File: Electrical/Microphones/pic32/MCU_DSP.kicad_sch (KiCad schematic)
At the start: 28 parts, among them IC1 PIC32MK0128MCA048-I_Y8X, J1 Conn_01x05_Pin, J2 Conn_01x06, J3 Conn_01x06, J4 Conn_01x05, J5 Conn_01x06, J6 Conn_01x05, J7 UART, SW1 B3F-1020, SW2 SW_SPDT, U1 GSF7002DW

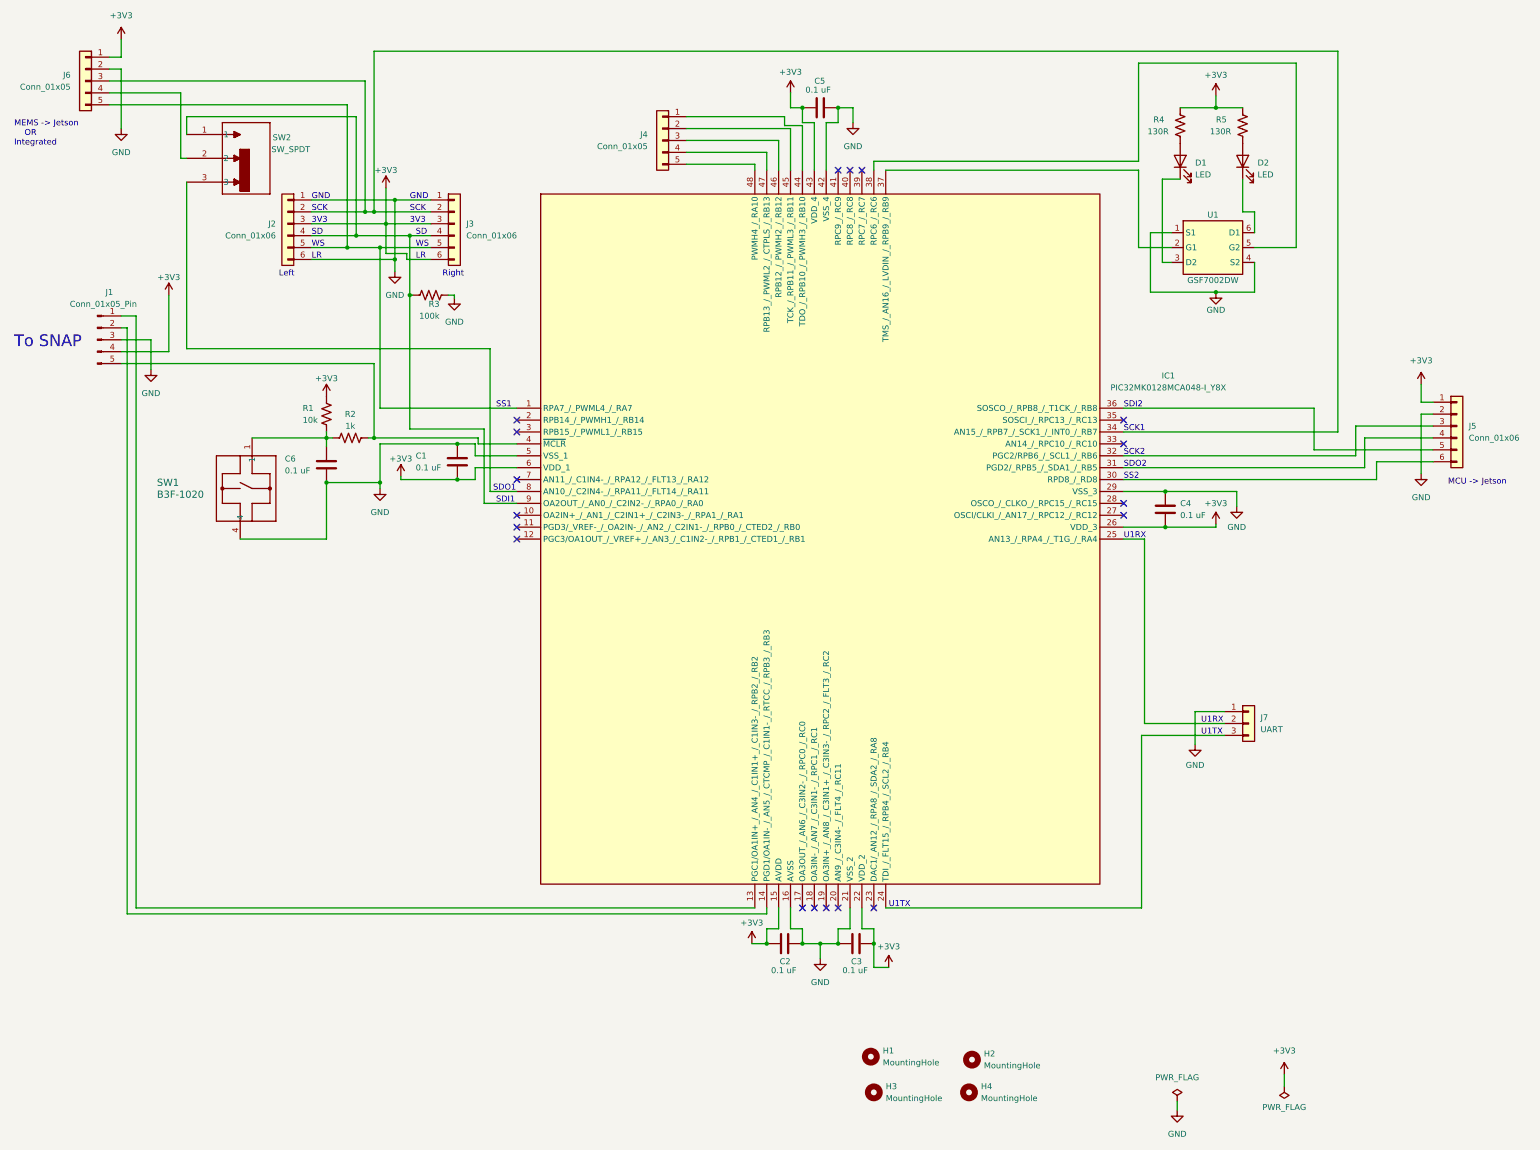
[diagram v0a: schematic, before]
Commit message: Add updated Mic MCU board
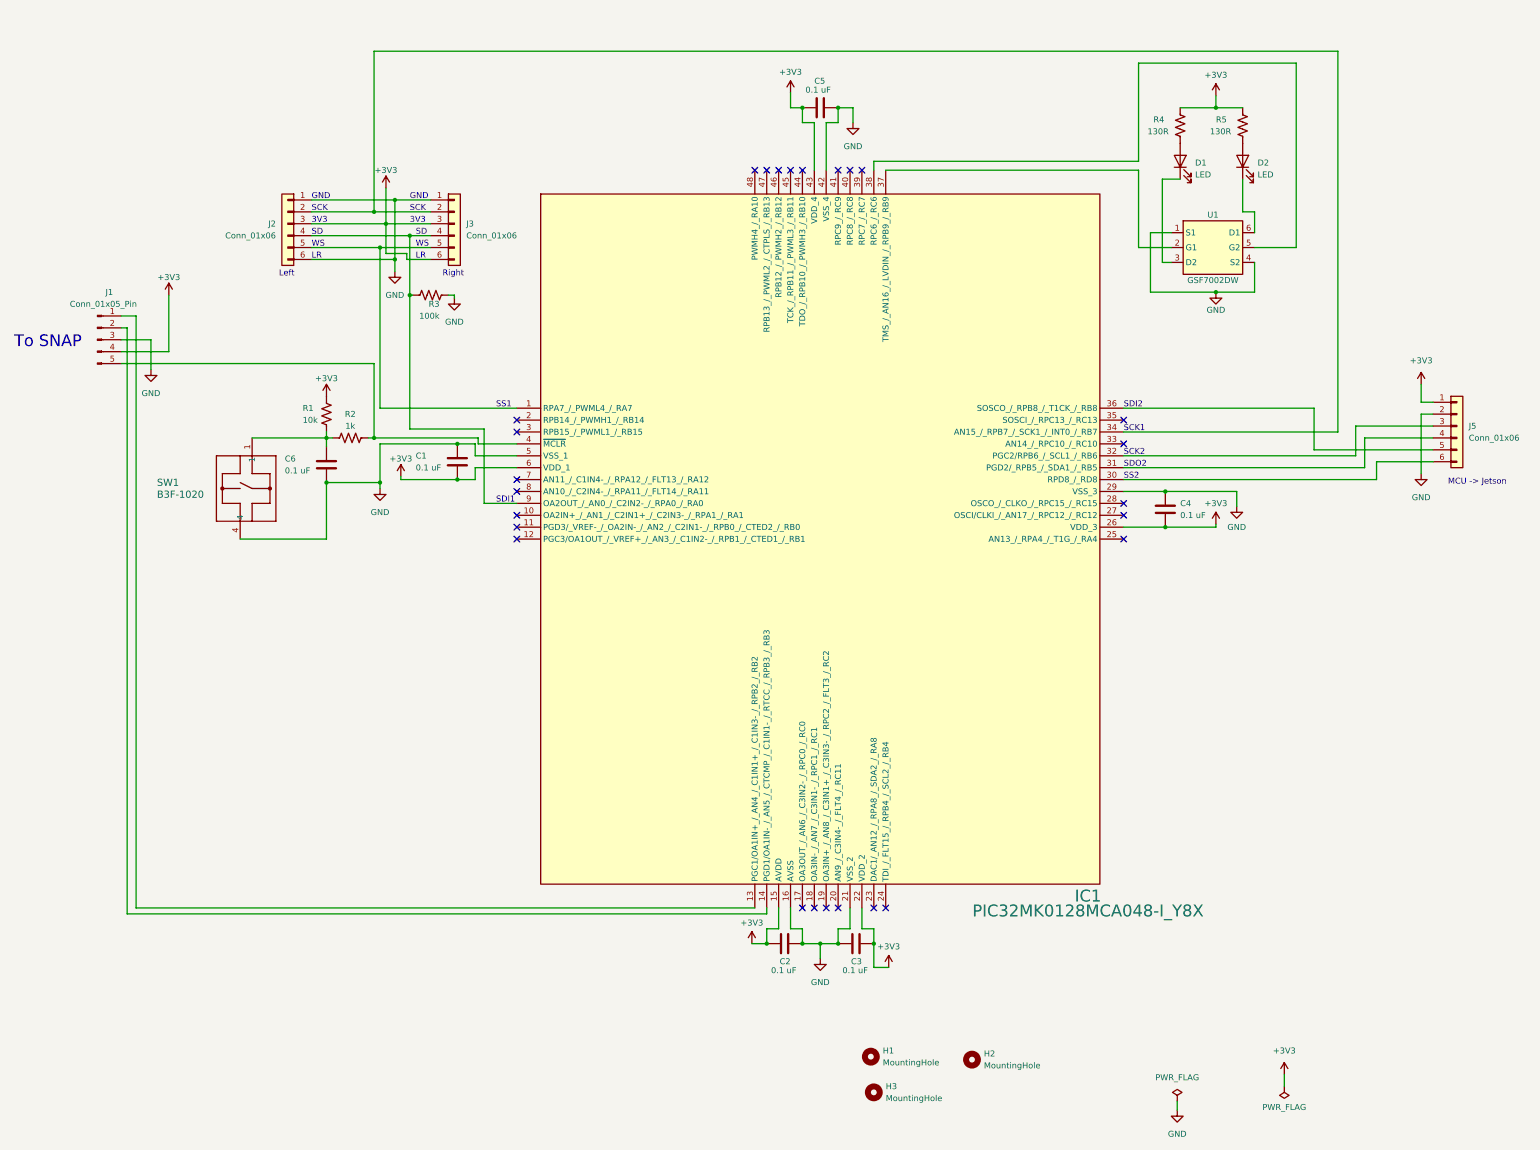
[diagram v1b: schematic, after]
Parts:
- removed H4: MountingHole, MountingHole:MountingHole_3.2mm_M3, symbol Mechanical:MountingHole
- removed J4: Conn_01x05, Connector_PinHeader_2.54mm:PinHeader_1x05_P2.54mm_Vertical, symbol Connector_Generic:Conn_01x05
- removed J6: Conn_01x05, Connector_Molex:Molex_KK-254_AE-6410-05A_1x05_P2.54mm_Vertical, symbol Connector_Generic:Conn_01x05
- removed J7: UART, Connector_PinHeader_2.54mm:PinHeader_1x03_P2.54mm_Vertical, symbol Connector_Generic:Conn_01x03
- removed SW2: SW_SPDT, custom_footprints:SPDT_OS102011_CNK, symbol Matts_Library:OS102011MS2QN1
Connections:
- no-connect marks 18 -> 26
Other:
- note removed: "MEMS -> Jetson OR Integrated"
- note removed: "SDO1"
- note removed: "U1RX"
- note removed: "U1TX"
- title: Test sheet -> Audio Processing Board

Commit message: Update some parts
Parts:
- D1, D2: Mfr Würth Elektronik -> Harvatek Corporation; Mfr P/N 150080RS75000 -> B1701URO-20D000114U1930; Supplier 1 P/N 732-4984-1-ND -> 3147-B1701URO-20D000114U1930CT-ND
- J2, J3, J5: Mfr P/N 1718560006 -> 0022232061; Supplier 1 P/N WM10156-ND -> WM4204-ND
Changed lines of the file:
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@@
 			)
 		)
-		(property "Mfr P/N" "1718560006"
+		(property "Mfr P/N" "0022232061"
 			(at 83.82 62.23 0)
 			(effects
@@
 			)
 		)
-		(property "Supplier 1 P/N" "WM10156-ND"
+		(property "Supplier 1 P/N" "WM4204-ND"
 			(at 83.82 62.23 0)
 			(effects
@@
 			)
 		)
-		(property "Mfr" "Würth Elektronik"
+		(property "Mfr" "Harvatek Corporation "
 			(at 274.32 48.895 0)
 			(effects
@@
 			)
 		)
-		(property "Mfr P/N" "150080RS75000"
+		(property "Mfr P/N" "B1701URO-20D000114U1930 "
 			(at 274.32 48.895 0)
 			(effects
@@
 			)
 		)
-		(property "Supplier 1 P/N" "732-4984-1-ND"
+		(property "Supplier 1 P/N" "3147-B1701URO-20D000114U1930CT-ND "
 			(at 274.32 48.895 0)
 			(effects
@@
 			)
 		)
-		(property "Mfr" "Würth Elektronik"
+		(property "Mfr" "Harvatek Corporation "
 			(at 287.655 48.895 0)
 			(effects
@@
 			)
 		)
-		(property "Mfr P/N" "150080RS75000"
+		(property "Mfr P/N" "B1701URO-20D000114U1930 "
 			(at 287.655 48.895 0)
 			(effects
@@
 			)
 		)
-		(property "Supplier 1 P/N" "732-4984-1-ND"
+		(property "Supplier 1 P/N" "3147-B1701URO-20D000114U1930CT-ND "
 			(at 287.655 48.895 0)
 			(effects
@@
 			)
 		)
-		(property "Mfr P/N" "1718560006"
+		(property "Mfr P/N" "0022232061"
 			(at 333.375 105.41 0)
 			(effects
@@
 			)
 		)
-		(property "Supplier 1 P/N" "WM10156-ND"
+		(property "Supplier 1 P/N" "WM4204-ND"
 			(at 333.375 105.41 0)
 			(effects
@@
 			)
 		)
-		(property "Mfr P/N" "1718560006"
+		(property "Mfr P/N" "0022232061"
 			(at 119.38 62.23 0)
 			(effects
@@
 			)
 		)
-		(property "Supplier 1 P/N" "WM10156-ND"
+		(property "Supplier 1 P/N" "WM4204-ND"
 			(at 119.38 62.23 0)
 			(effects
